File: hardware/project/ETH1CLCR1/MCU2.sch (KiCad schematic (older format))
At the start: 30 parts, among them J1301 20021111-00010T4LF, U1301 STM32H743ZI, U1302 24LC08B-E/MS, Y1301 NX3225GD-8MHZ-STD-CRA-3

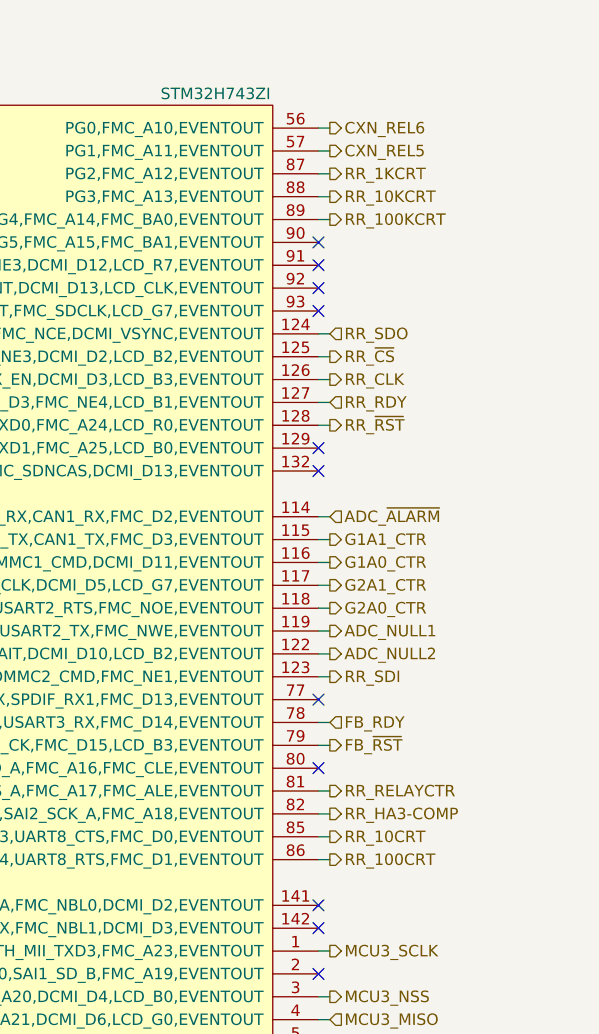
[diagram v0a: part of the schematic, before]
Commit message: Was able to set the SPI3 (MCU2) to run with 80 MHZ clock speed with AD7380. Using HAL lib for SPI and GPIO, too slow switching. Need to change to LL with DMA.
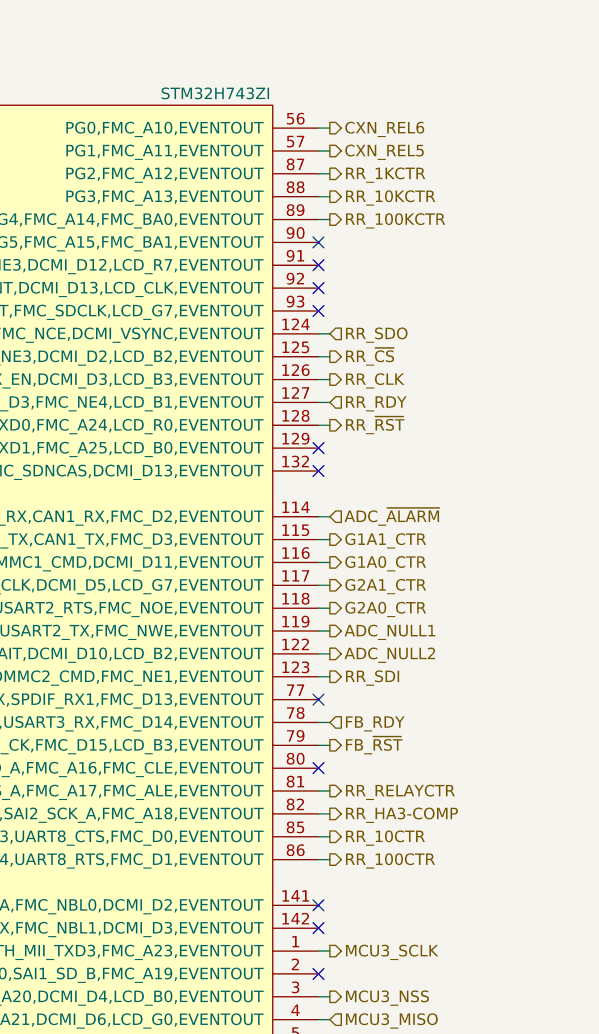
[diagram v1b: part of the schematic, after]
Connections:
- net RR_100CRT renamed RR_100CTR
- net RR_100KCRT renamed RR_100KCTR
- net RR_10CRT renamed RR_10CTR
- net RR_10KCRT renamed RR_10KCTR
- net RR_1KCRT renamed RR_1KCTR
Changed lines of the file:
@@
 CXN_REL4
 Text HLabel 14350 4500 2    50   Output ~ 0
-RR_100CRT
+RR_100CTR
 Text HLabel 14350 4400 2    50   Output ~ 0
-RR_10CRT
+RR_10CTR
 Text HLabel 14350 1500 2    50   Output ~ 0
-RR_1KCRT
+RR_1KCTR
 Text HLabel 14350 1600 2    50   Output ~ 0
-RR_10KCRT
+RR_10KCTR
 Text HLabel 14350 1700 2    50   Output ~ 0
-RR_100KCRT
+RR_100KCTR
 Text HLabel 14350 4200 2    50   Output ~ 0
 RR_RELAYCTR
